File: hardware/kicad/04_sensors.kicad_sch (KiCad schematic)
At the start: 0 parts

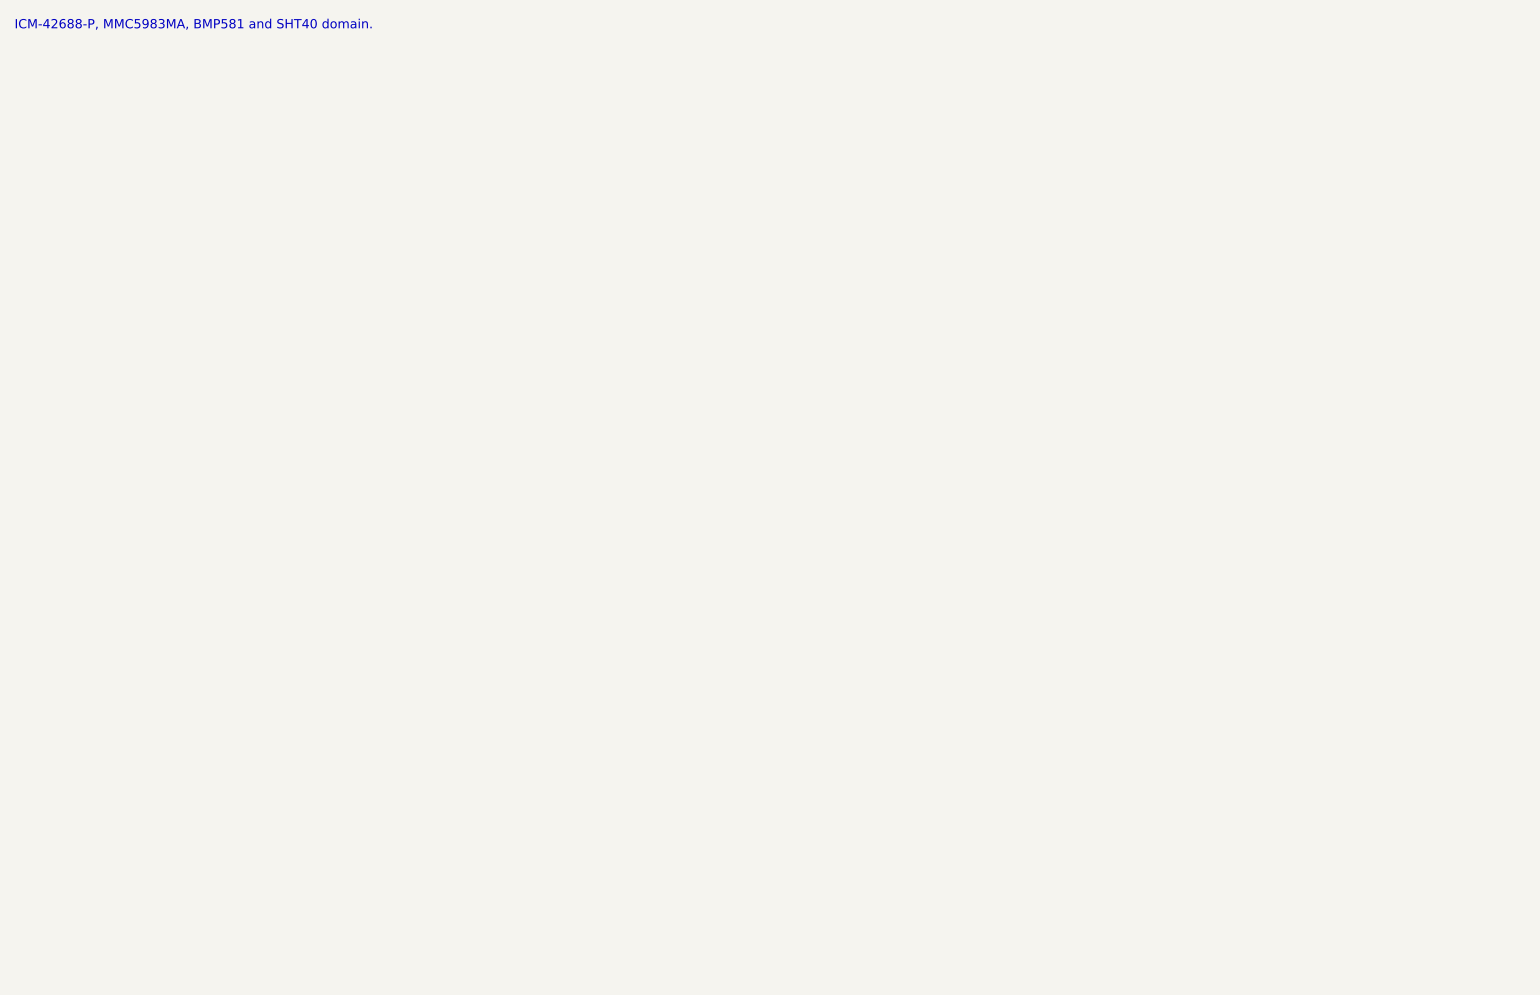
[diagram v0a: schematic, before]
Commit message: hardware: add reviewed sensor subset
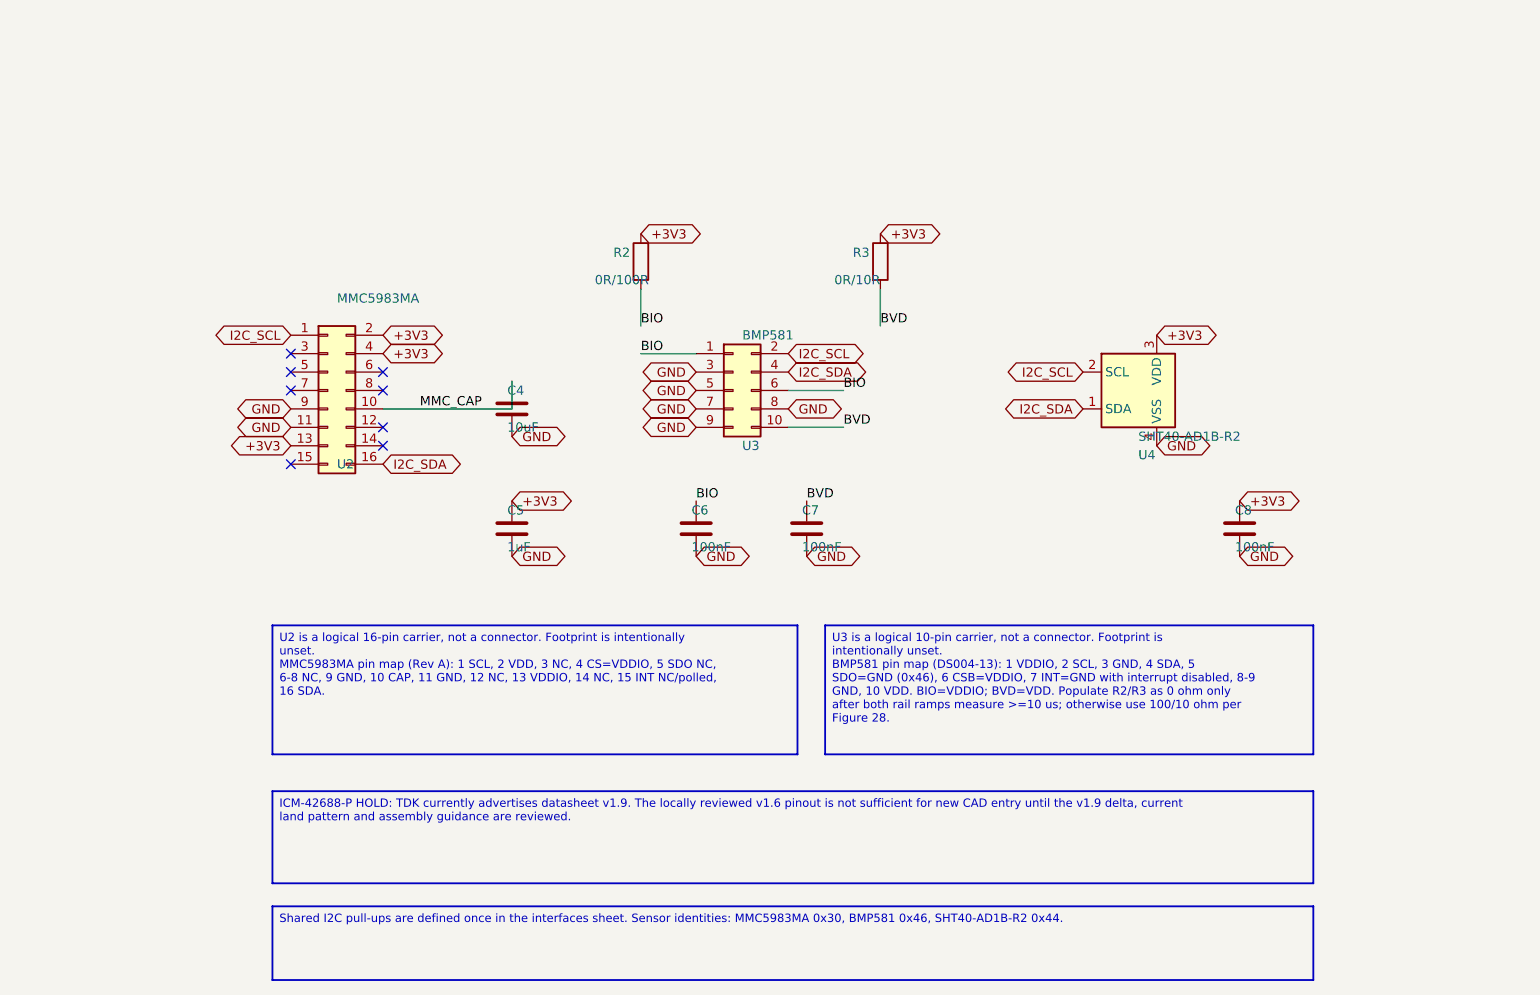
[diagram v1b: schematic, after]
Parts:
- added C4: 10uF, Capacitor_SMD:C_0805_2012Metric, symbol Device:C
- added C5: 1uF, Capacitor_SMD:C_0603_1608Metric, symbol Device:C
- added C6, C7, C8: 100nF, Capacitor_SMD:C_0603_1608Metric, symbol Device:C
- added R2: 0R/100R, Resistor_SMD:R_0603_1608Metric, symbol Device:R
- added R3: 0R/10R, Resistor_SMD:R_0603_1608Metric, symbol Device:R
- added U2: MMC5983MA, symbol Connector_Generic:Conn_02x08_Odd_Even
- added U3: BMP581, symbol Connector_Generic:Conn_02x05_Odd_Even
- added U4: SHT40-AD1B-R2, Sensor_Humidity:Sensirion_DFN-4_1.5x1.5mm_P0.8mm_SHT4x_NoCentralPad, symbol Sensor_Humidity:SHT4x
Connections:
- new net +3V3: C5.2, C8.2, R2.1, R3.1, U2.13 (Pin_13), U2.2 (Pin_2), U2.4 (Pin_4), U4.3 (VDD)
- new net BIO: C6.2, R2.2, U3.1 (Pin_1), U3.6 (Pin_6)
- new net BVD: C7.2, R3.2, U3.10 (Pin_10)
- new net GND: C4.1, C5.1, C6.1, C7.1, C8.1, U2.11 (Pin_11), U2.9 (Pin_9), U3.3 (Pin_3), U3.5 (Pin_5), U3.7 (Pin_7), U3.8 (Pin_8), U3.9 (Pin_9), U4.4 (VSS)
- new net I2C_SCL: U2.1 (Pin_1), U3.2 (Pin_2), U4.2 (SCL)
- new net I2C_SDA: U2.16 (Pin_16), U3.4 (Pin_4), U4.1 (SDA)
- new net MMC_CAP: C4.2, U2.10 (Pin_10)
- no-connect marks 0 -> 8
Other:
- note removed: "ICM-42688-P, MMC5983MA, BMP581 and SHT40 domain."
- title: 04 Sensors -> 04 Sensors - reviewed subset
